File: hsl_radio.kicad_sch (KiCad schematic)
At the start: 71 parts, among them J2 CC Prog/Debug, J4 UART1, J5 Control Outputs, J6 ANT, U1 AP62300TWU-7, U2 CC1110, U3 SF2446E, U5 TLV803S, U6 PE4259, U7 0433BM15A0001, U8 FT5HN 27MHz

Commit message: Preparing for JLCPCB
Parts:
- U1: footprint TSOT26-WU_DIO -> openlst:TSOT26-WU_DIO

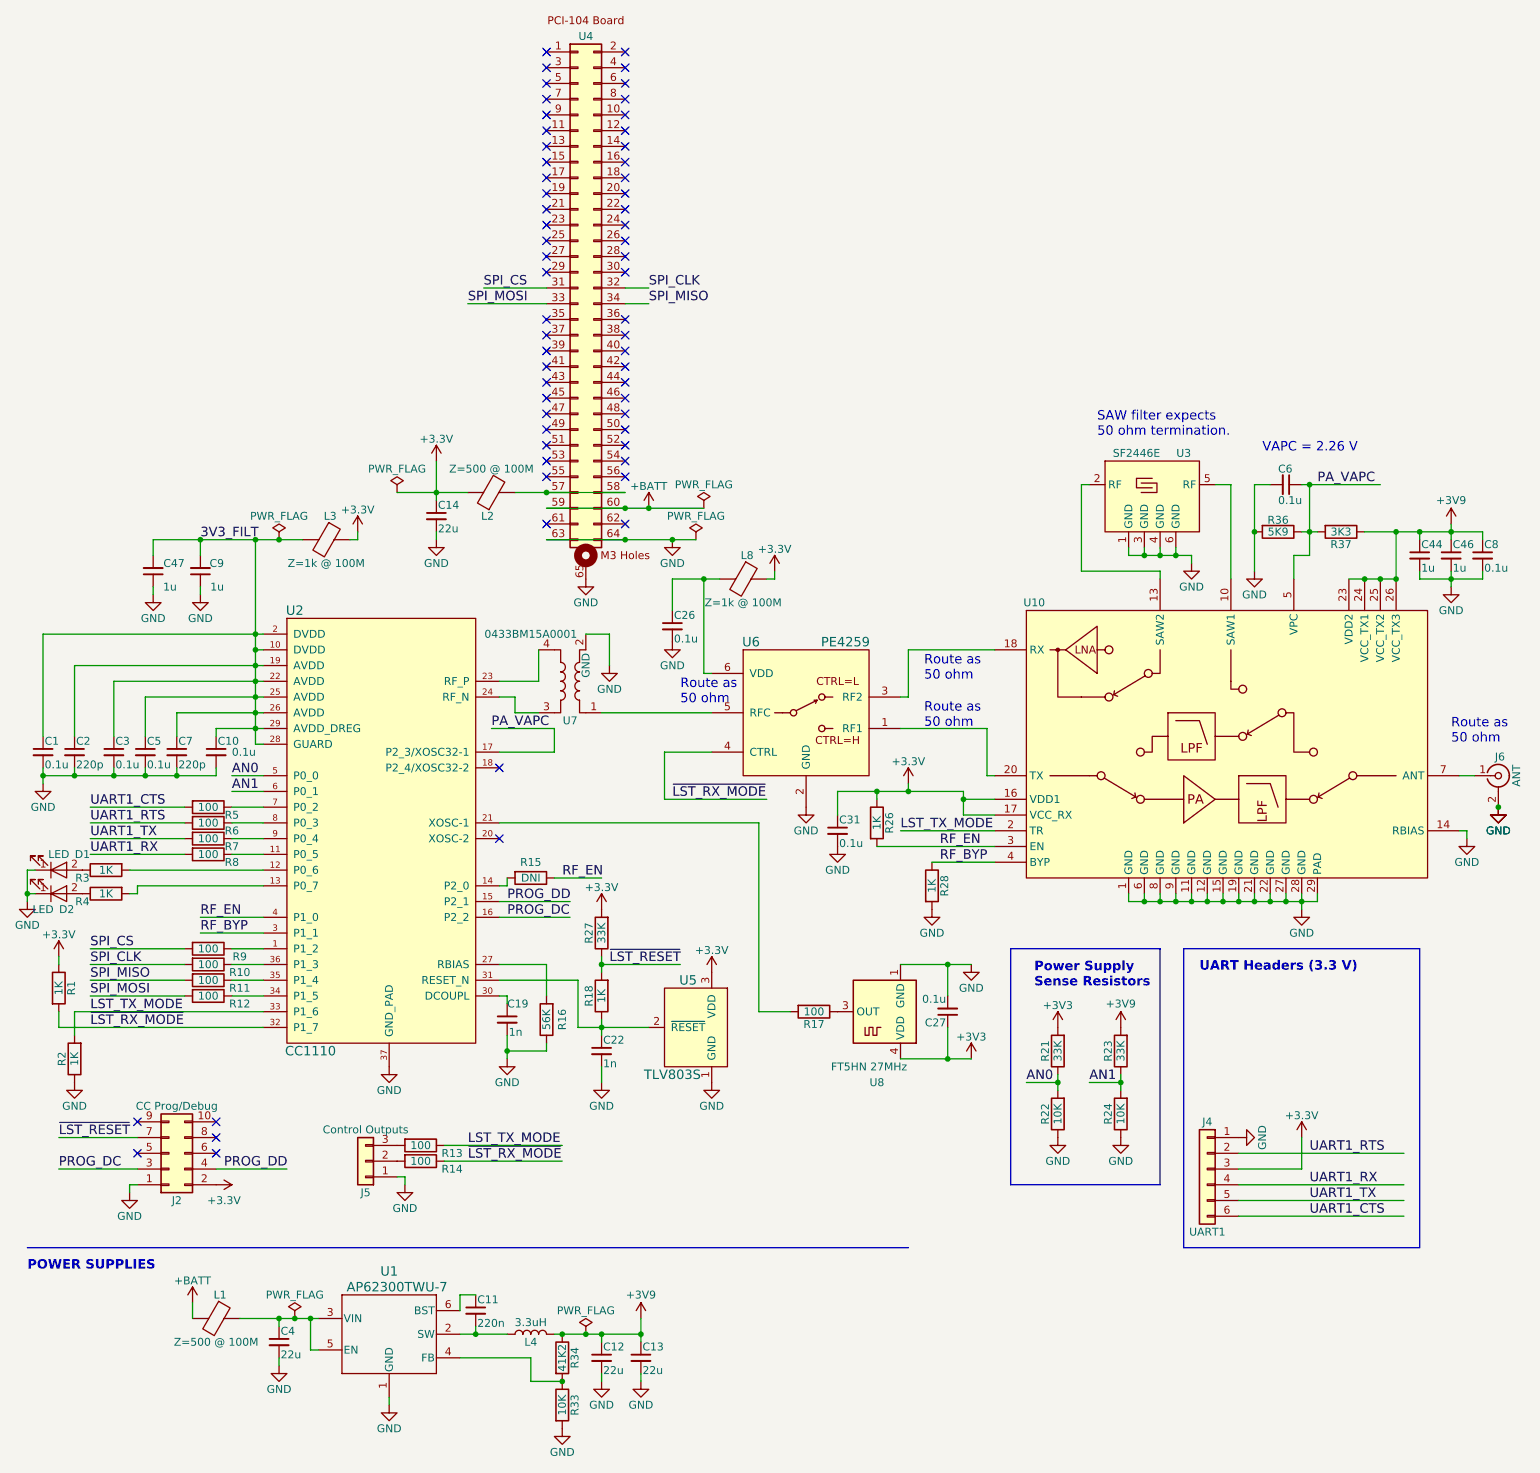
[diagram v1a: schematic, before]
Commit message: Added test points
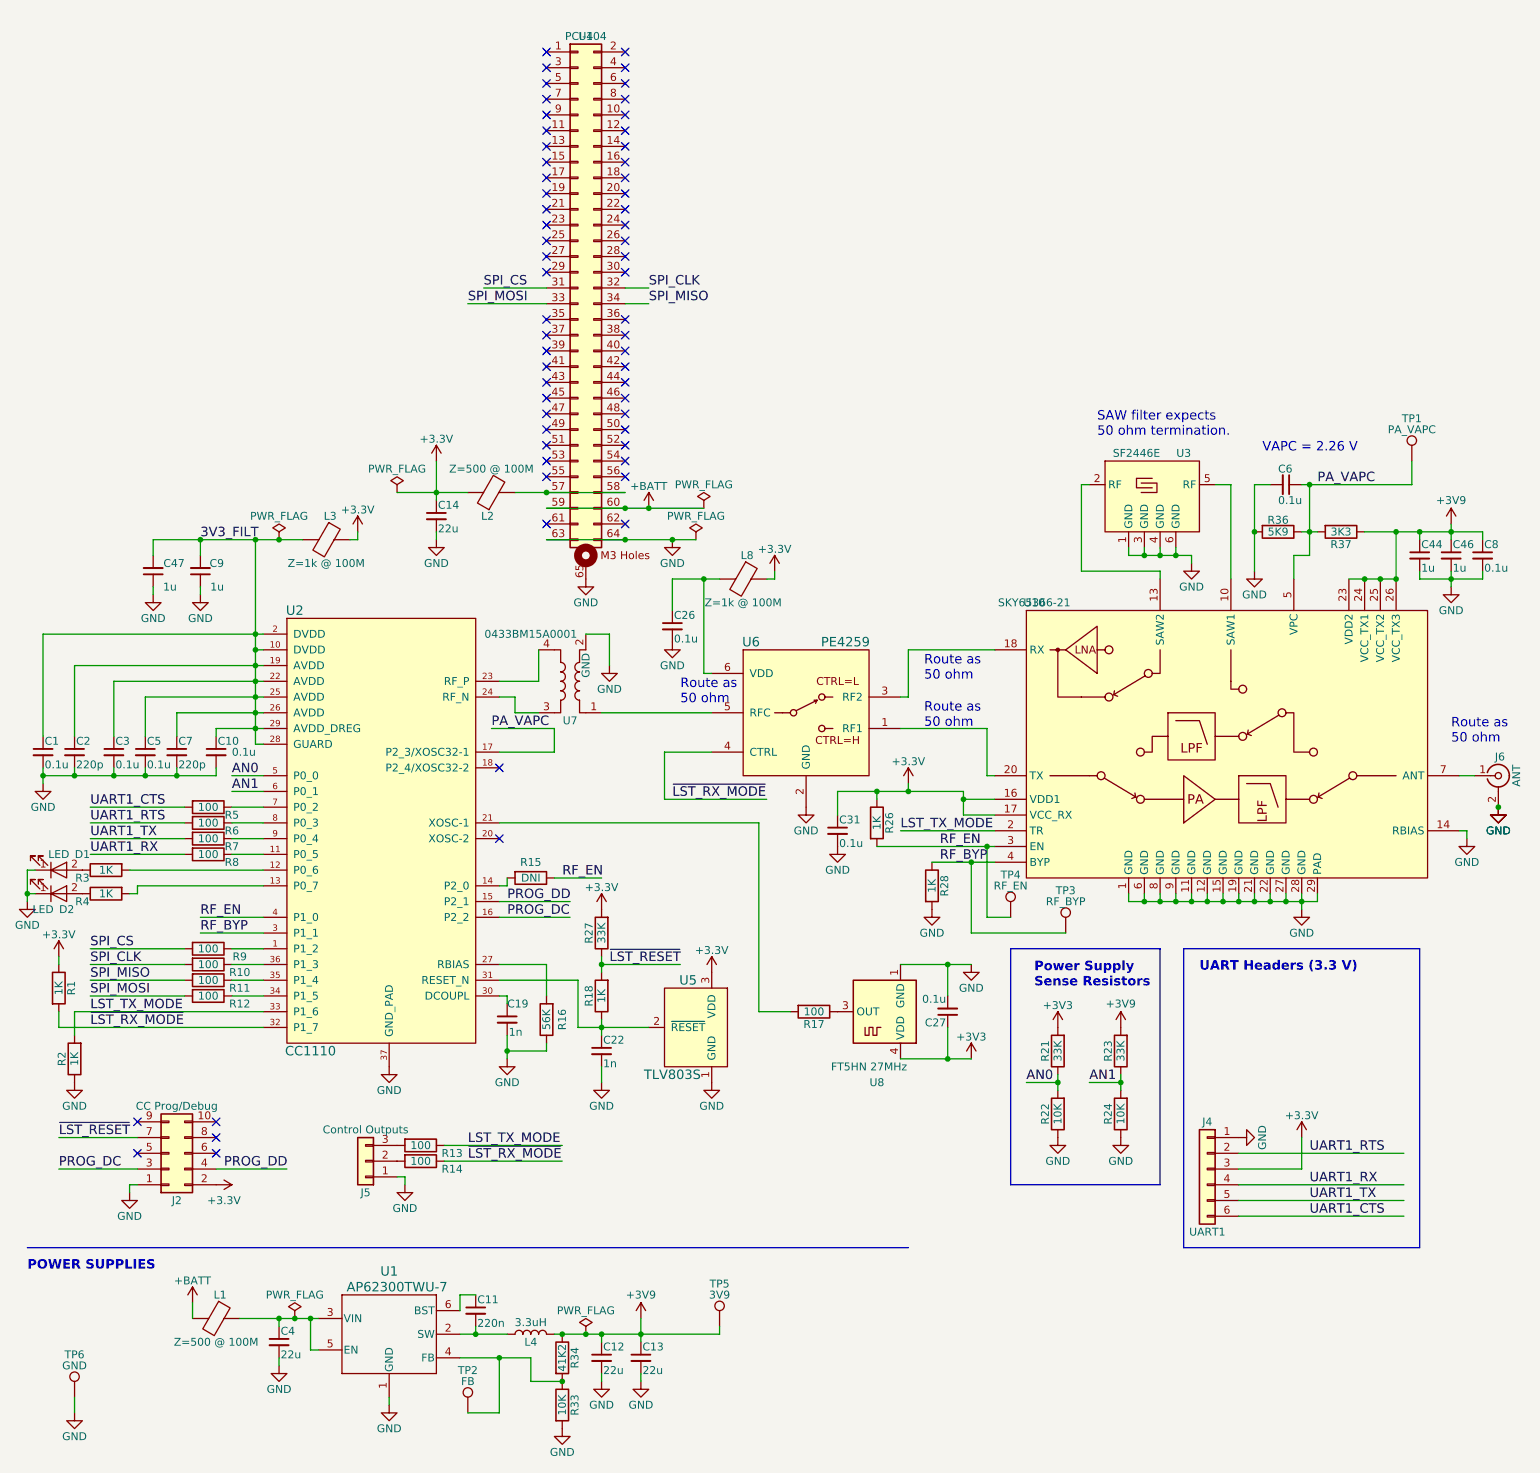
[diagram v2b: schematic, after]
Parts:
- added TP1: PA_VAPC, TestPoint:TestPoint_Pad_D2.0mm, symbol Connector:TestPoint
- added TP2: FB, TestPoint:TestPoint_Pad_D2.0mm, symbol Connector:TestPoint
- added TP3: RF_BYP, TestPoint:TestPoint_Pad_D2.0mm, symbol Connector:TestPoint
- added TP4: RF_EN, TestPoint:TestPoint_Pad_D2.0mm, symbol Connector:TestPoint
- added TP5: 3V9, TestPoint:TestPoint_Pad_D2.0mm, symbol Connector:TestPoint
- added TP6: GND, TestPoint:TestPoint_Pad_D2.0mm, symbol Connector:TestPoint
- U10: value ~ -> SKY65366-21
- U4: value ~ -> PCI-104
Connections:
- net +3V9: now also TP5.1
- net GND: now also TP6.1
- net PA_VAPC: now also TP1.1
- net RF_BYP: now also TP3.1
- net RF_EN: now also TP4.1
- net at R33.1, R34.2, U1.4 (FB): now also TP2.1

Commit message: Finalizing for JLCPCB
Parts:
- U5: footprint archive:SOT-23 -> Package_TO_SOT_SMD:SOT-23
- U6: footprint archive:SOT-363_SC-70-6 -> Package_TO_SOT_SMD:SOT-363_SC-70-6
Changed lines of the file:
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@@
       (effects (font (size 1.524 1.524)))
     )
-    (property "Footprint" "archive:SOT-23" (at 124.46 133.35 0)
-      (effects (font (size 1.524 1.524)) hide)
-    )
-    (property "Datasheet" "http://www.ti.com/lit/ds/symlink/tlv803.pdf" (at 124.46 133.35 0)
+    (property "Footprint" "Package_TO_SOT_SMD:SOT-23" (at 124.46 133.35 0)
+      (effects (font (size 1.524 1.524)) hide)
+    )
+    (property "Datasheet" "https://www.ti.com/lit/ds/symlink/tlv803.pdf?ts=1708710745708&ref_url=https%253A%252F%252Fwww.google.com%252F" (at 124.46 133.35 0)
       (effects (font (size 1.524 1.524)) hide)
     )
@@
       (effects (font (size 1.524 1.524)))
     )
-    (property "Footprint" "archive:SOT-363_SC-70-6" (at 142.24 96.52 0)
-      (effects (font (size 1.524 1.524)) hide)
-    )
-    (property "Datasheet" "http://www.psemi.com/pdf/datasheets/pe4259ds.pdf" (at 142.24 96.52 0)
-      (effects (font (size 1.524 1.524)) hide)
-    )
+    (property "Footprint" "Package_TO_SOT_SMD:SOT-363_SC-70-6" (at 142.24 96.52 0)
+      (effects (font (size 1.524 1.524)) hide)
+    )
+    (property "Datasheet" "https://www.psemi.com/pdf/datasheets/pe4259ds.pdf" (at 142.24 96.52 0)
+      (effects (font (size 1.524 1.524)) hide)
+    )
